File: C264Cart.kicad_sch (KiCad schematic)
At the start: 13 parts, among them U1 27C040, U3 264-Exp-Port

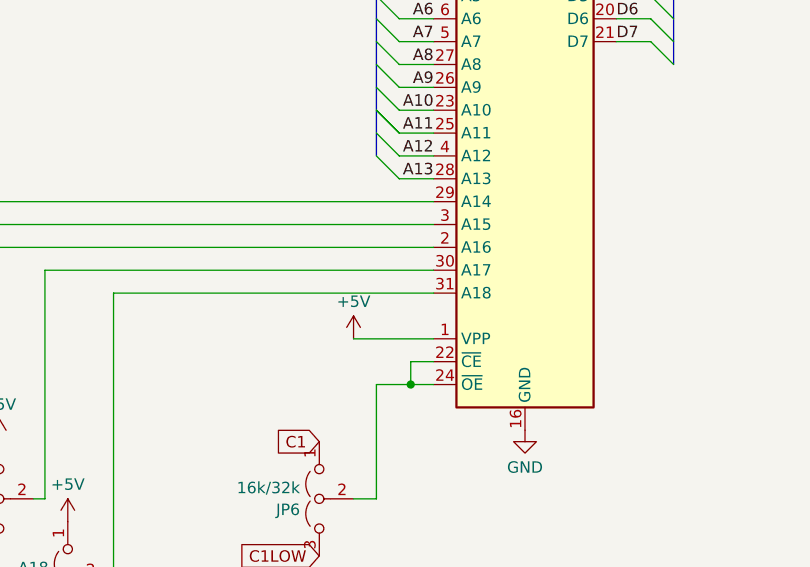
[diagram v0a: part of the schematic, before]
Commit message: Working to use a single 'modern' 27C512-27C040 EEPROM.
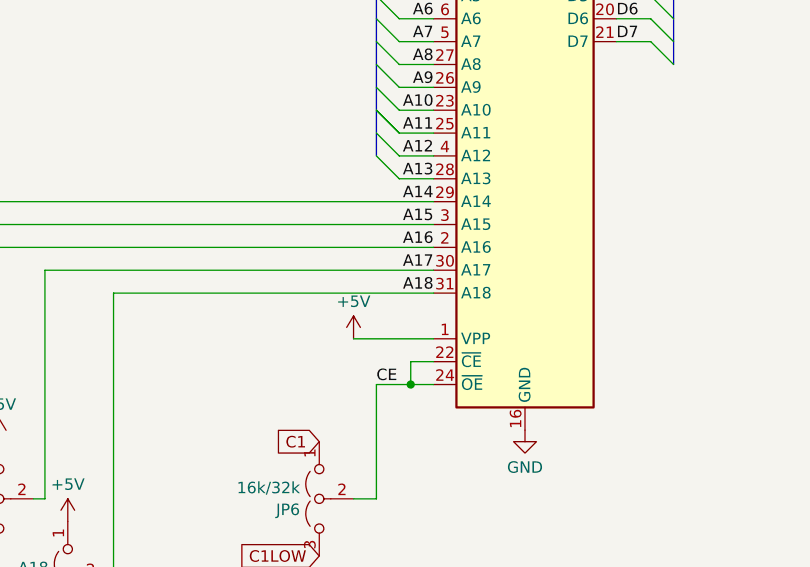
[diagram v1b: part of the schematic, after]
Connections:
- net A18: now reaches JP5.2 (C), U1.31 (A18)
- net A17: now reaches JP4.2 (C), U1.30 (A17)
- net A14: now reaches JP1.2 (C), JP7.2 (C), U1.29 (A14)
- net A16: now reaches JP3.2 (C), U1.2 (A16)
- net A15: now reaches JP2.2 (C), U1.3 (A15)
- net CE: now reaches JP6.2 (C), U1.22 (~{CE}), U1.24 (~{OE})
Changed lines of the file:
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@@
+    (effects (font (size 1.27 1.27)) (justify right bottom))
+  )
+  (label "A14" (at 212.09 86.36 180) (fields_autoplaced)
     (effects (font (size 1.27 1.27)) (justify right bottom))
   )
@@
     (effects (font (size 1.27 1.27)) (justify right bottom))
   )
+  (label "A18" (at 212.09 96.52 180) (fields_autoplaced)
+    (effects (font (size 1.27 1.27)) (justify right bottom))
+  )
+  (label "CE" (at 205.74 106.68 0) (fields_autoplaced)
+    (effects (font (size 1.27 1.27)) (justify left bottom))
+  )
   (label "A3" (at 212.09 58.42 180) (fields_autoplaced)
+    (effects (font (size 1.27 1.27)) (justify right bottom))
+  )
+  (label "A17" (at 212.09 93.98 180) (fields_autoplaced)
     (effects (font (size 1.27 1.27)) (justify right bottom))
   )
@@
   )
   (label "A8" (at 212.09 71.12 180) (fields_autoplaced)
+    (effects (font (size 1.27 1.27)) (justify right bottom))
+  )
+  (label "A15" (at 212.09 88.9 180) (fields_autoplaced)
     (effects (font (size 1.27 1.27)) (justify right bottom))
   )
@@
     (effects (font (size 1.27 1.27)) (justify right bottom))
   )
+  (label "A16" (at 212.09 91.44 180) (fields_autoplaced)
+    (effects (font (size 1.27 1.27)) (justify right bottom))
+  )

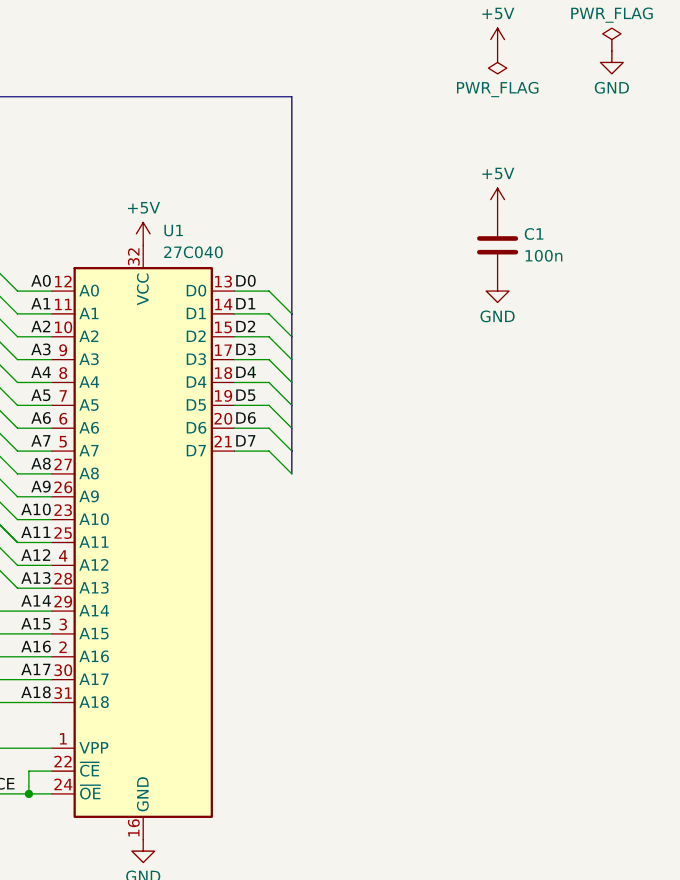
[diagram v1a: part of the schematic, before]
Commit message: Working to use a single 'modern' 27C512-27C040 EEPROM.
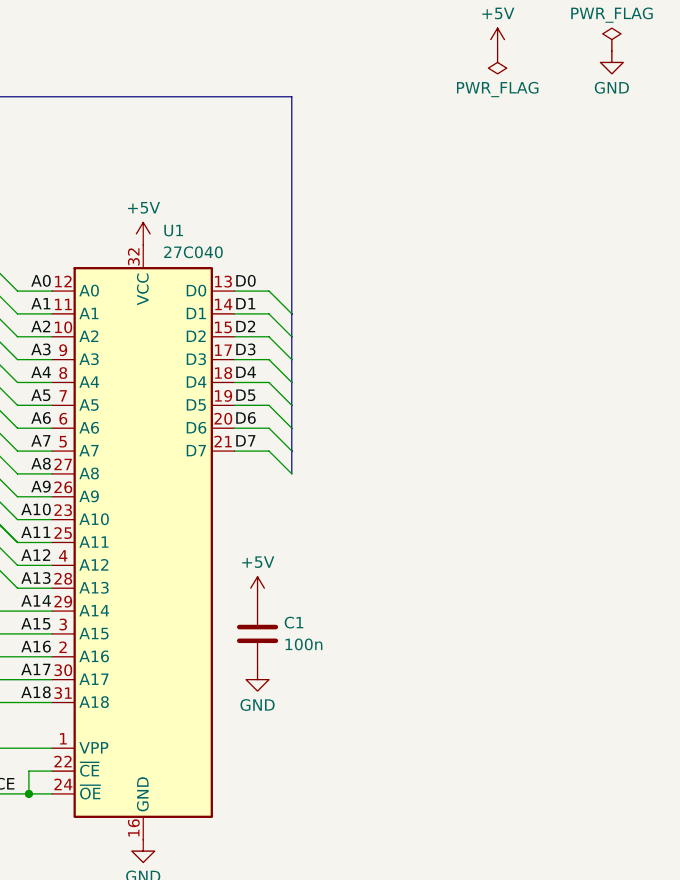
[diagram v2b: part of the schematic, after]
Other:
- title: C264Cart - Artwork No. 310189 Replica -> C264Cart
- moved on the sheet: C1
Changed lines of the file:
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@@
   (paper "A4")
   (title_block
-    (title "C264Cart - Artwork No. 310189 Replica")
+    (title "C264Cart")
     (date "2023-11-13")
     (rev "1")
@@
     (comment 1 "Creative Commons Attribution-NonCommercial-ShareAlike 4.0 International License.")
     (comment 2 "This work is licensed under a")
-    (comment 4 "Replica Commodore Cartridge PCB for C16 and Plus/4, Artwork No. 310189 Rev.1")
   )
   (junction (at 146.05 86.36) (diameter 0) (color 0 0 0 0)
@@
     )
   )
-  (symbol (lib_id "power:GND") (at 261.62 49.53 0) (unit 1)
-    (in_bom yes) (on_board yes) (dnp no) (fields_autoplaced)
-    (property "Reference" "#PWR016" (at 261.62 55.88 0)
-      (effects (font (size 1.27 1.27)) hide)
-    )
-    (property "Value" "GND" (at 261.62 53.6631 0)
-      (effects (font (size 1.27 1.27)))
-    )
-    (property "Footprint" "" (at 261.62 49.53 0)
-      (effects (font (size 1.27 1.27)) hide)
-    )
-    (property "Datasheet" "" (at 261.62 49.53 0)
+  (symbol (lib_id "power:GND") (at 234.95 92.71 0) (unit 1)
+    (in_bom yes) (on_board yes) (dnp no) (fields_autoplaced)
+    (property "Reference" "#PWR016" (at 234.95 99.06 0)
+      (effects (font (size 1.27 1.27)) hide)
+    )
+    (property "Value" "GND" (at 234.95 96.8431 0)
+      (effects (font (size 1.27 1.27)))
+    )
+    (property "Footprint" "" (at 234.95 92.71 0)
+      (effects (font (size 1.27 1.27)) hide)
+    )
+    (property "Datasheet" "" (at 234.95 92.71 0)
       (effects (font (size 1.27 1.27)) hide)
     )
@@
     )
   )
-  (symbol (lib_id "Device:C") (at 261.62 45.72 0) (unit 1)
-    (in_bom yes) (on_board yes) (dnp no) (fields_autoplaced)
-    (property "Reference" "C1" (at 264.541 44.5079 0)
-      (effects (font (size 1.27 1.27)) (justify left))
-    )
-    (property "Value" "100n" (at 264.541 46.9321 0)
-      (effects (font (size 1.27 1.27)) (justify left))
-    )
-    (property "Footprint" "Capacitor_THT:C_Disc_D6.0mm_W2.5mm_P5.00mm" (at 262.5852 49.53 0)
-      (effects (font (size 1.27 1.27)) hide)
-    )
-    (property "Datasheet" "~" (at 261.62 45.72 0)
+  (symbol (lib_id "Device:C") (at 234.95 88.9 0) (unit 1)
+    (in_bom yes) (on_board yes) (dnp no) (fields_autoplaced)
+    (property "Reference" "C1" (at 237.871 87.6879 0)
+      (effects (font (size 1.27 1.27)) (justify left))
+    )
+    (property "Value" "100n" (at 237.871 90.1121 0)
+      (effects (font (size 1.27 1.27)) (justify left))
+    )
+    (property "Footprint" "Capacitor_THT:C_Disc_D6.0mm_W2.5mm_P5.00mm" (at 235.9152 92.71 0)
+      (effects (font (size 1.27 1.27)) hide)
+    )
+    (property "Datasheet" "~" (at 234.95 88.9 0)
       (effects (font (size 1.27 1.27)) hide)
     )
@@
     )
   )
-  (symbol (lib_id "power:+5V") (at 261.62 41.91 0) (unit 1)
-    (in_bom yes) (on_board yes) (dnp no) (fields_autoplaced)
-    (property "Reference" "#PWR015" (at 261.62 45.72 0)
-      (effects (font (size 1.27 1.27)) hide)
-    )
-    (property "Value" "+5V" (at 261.62 37.7769 0)
-      (effects (font (size 1.27 1.27)))
-    )
-    (property "Footprint" "" (at 261.62 41.91 0)
-      (effects (font (size 1.27 1.27)) hide)
-    )
-    (property "Datasheet" "" (at 261.62 41.91 0)
-      (effects (font (size 1.27 1.27)) hide)
-    )
+  (symbol (lib_id "power:+5V") (at 234.95 85.09 0) (unit 1)
+    (in_bom yes) (on_board yes) (dnp no) (fields_autoplaced)
+    (property "Reference" "#PWR015" (at 234.95 88.9 0)
+      (effects (font (size 1.27 1.27)) hide)
+    )
+    (property "Value" "+5V" (at 234.95 80.9569 0)
+      (effects (font (size 1.27 1.27)))
+    )
+    (property "Footprint" "" (at 234.95 85.09 0)
+      (effects (font (size 1.27 1.27)) hide)
+    )
+    (property "Datasheet" "" (at 234.95 85.09 0)
+      (effects (font (size 1.27 1.27)) hide)
+    )
